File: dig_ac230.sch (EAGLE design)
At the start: 134 parts, among them IC1 74HC595D, IC101 ATMEGA32A-AU, IC102 DS1337S, IC103 MAX487CSA, IC104 74HC166D, IC2 LTV-356T, IC3 LTV-356T, IC4 LTV-356T, IC5 LTV-356T, IC6 LTV-356T, IC7 LTV-356T, IC8 LTV-356T, IC9 LTV-356T, K301 S202S02, K302 S202S02, K303 S202S02, K304 S202S02, K305 S202S02, K306 S202S02, K307 S202S02, K308 S202S02, Q1 32,768kHz, Q2 BCR191, Q3 BCR191, Q4 BCR191, Q5 BCR191, Q6 BCR191, Q7 BCR191, Q8 BCR191, Q9 BCR191, X1 RIA-73-02, X10 RIA-73-02, X11 RIA-73-02, X12 RIA-73-02, X2 RIA-73-02, X3 RIA-73-02, X4 RIA-73-02, X5 RIA-73-02, X6 RIA-73-02, X7 RIA-73-02, X8 RIA-73-02, X9 RIA-73-02

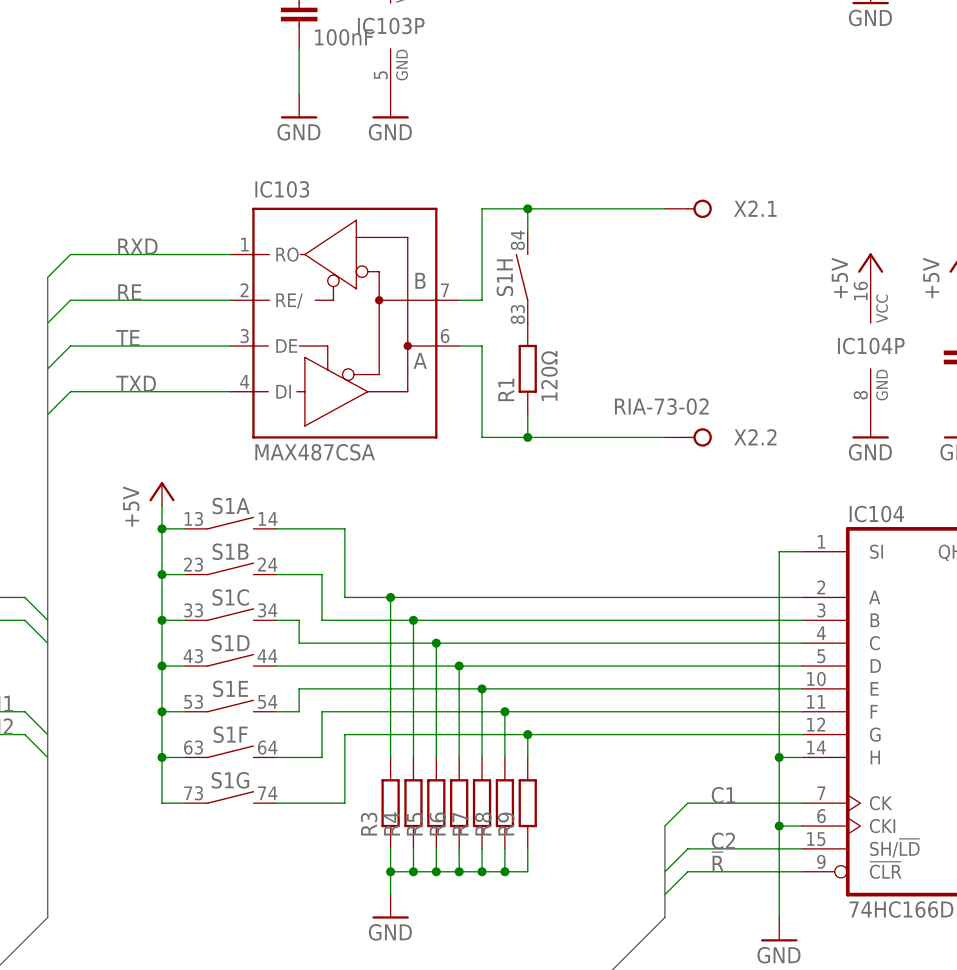
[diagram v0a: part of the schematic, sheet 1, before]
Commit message: Bauteile neu positoniert
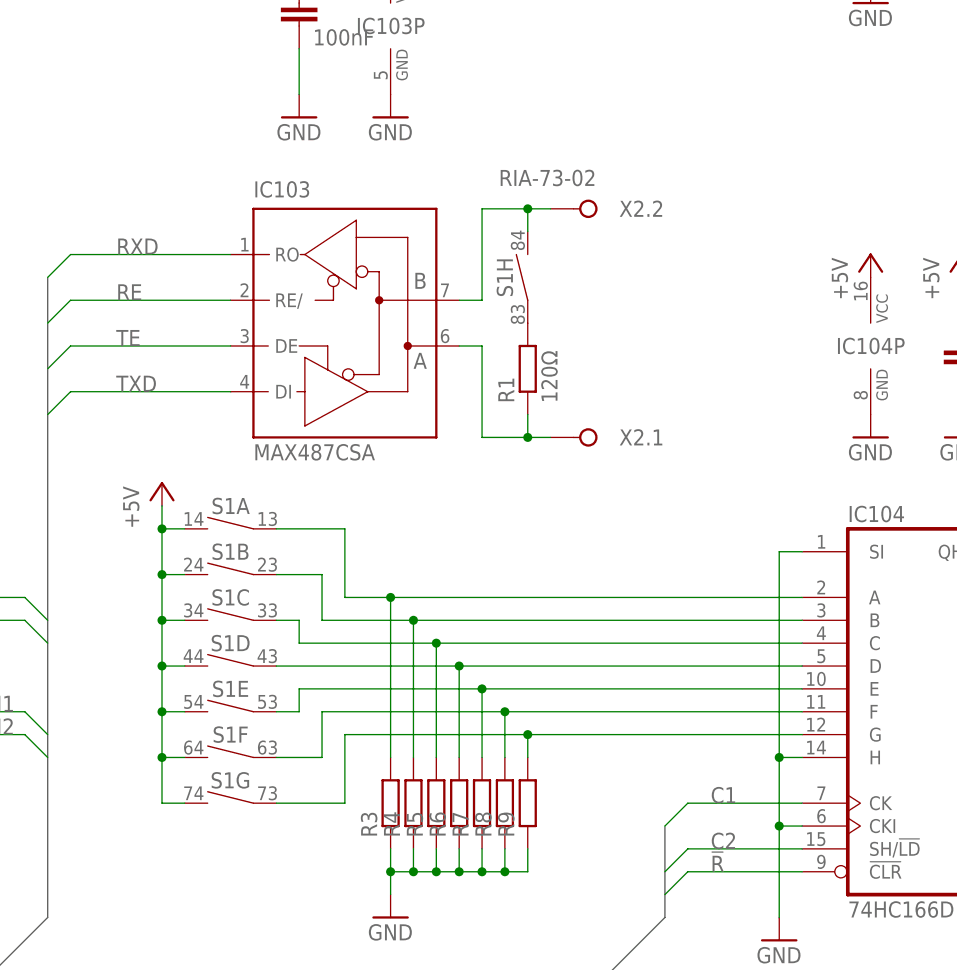
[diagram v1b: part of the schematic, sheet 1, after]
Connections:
- net GNDIO renamed N
- net N$90 renamed L
- net +5V: now also S1A.4, S1B.4, S1C.4, S1D.4, S1E.4, S1F.4, S1G.4; no longer S1A.3, S1B.3, S1C.3, S1D.3, S1E.3, S1F.3, S1G.3
- net N$20: now also X2.1.A; no longer X2.2.A
- net N$22: now also X2.2.A; no longer X2.1.A
- net N$26: now also S1A.3; no longer S1A.4
- net N$27: now also S1B.3; no longer S1B.4
- net N$28: now also S1C.3; no longer S1C.4
- net N$29: now also S1D.3; no longer S1D.4
- net N$30: now also S1E.3; no longer S1E.4
- net N$31: now also S1F.3; no longer S1F.4
- net N$32: now also S1G.3; no longer S1G.4
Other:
- moved on the sheet: X2.1, X2.2

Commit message: rev1 geroutet
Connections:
- net N$20: now also S1H.4; no longer R1.1
- net N$22: now also R1.1; no longer S1H.4
- net RE: now also IC101.(OC1A)PD5; no longer IC101.(OC1B)PD4
- net TE: now also IC101.(OC1B)PD4; no longer IC101.(OC1A)PD5
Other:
- moved on the sheet: R1, S1H
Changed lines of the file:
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@@
 <instance part="GND39" gate="1" x="292.1" y="149.86"/>
 <instance part="P+2" gate="1" x="83.82" y="167.64"/>
-<instance part="R1" gate="G$1" x="226.06" y="109.22" rot="R90"/>
+<instance part="R1" gate="G$1" x="226.06" y="119.38" rot="R270"/>
 <instance part="G1" gate="G$1" x="292.1" y="162.56"/>
 <instance part="V1" gate="G$1" x="226.06" y="175.26"/>
@@
 <instance part="S1" gate="F" x="193.04" y="66.04" rot="MR0"/>
 <instance part="S1" gate="G" x="193.04" y="60.96" rot="MR0"/>
-<instance part="S1" gate="H" x="226.06" y="119.38" rot="R90"/>
+<instance part="S1" gate="H" x="226.06" y="109.22" rot="R270"/>
 <instance part="IC104" gate="A" x="269.24" y="71.12"/>
 <instance part="R3" gate="G$1" x="210.82" y="60.96" rot="R90"/>
@@
 <wire x1="220.98" y1="111.76" x2="220.98" y2="101.6" width="0.1524" layer="91"/>
 <wire x1="220.98" y1="101.6" x2="226.06" y2="101.6" width="0.1524" layer="91"/>
-<pinref part="R1" gate="G$1" pin="1"/>
-<wire x1="226.06" y1="101.6" x2="226.06" y2="104.14" width="0.1524" layer="91"/>
 <pinref part="X2" gate=".1" pin="A"/>
-<wire x1="228.6" y1="101.6" x2="226.06" y2="101.6" width="0.1524" layer="91"/>
+<pinref part="S1" gate="H" pin="4"/>
+<wire x1="226.06" y1="101.6" x2="228.6" y2="101.6" width="0.1524" layer="91"/>
+<wire x1="226.06" y1="104.14" x2="226.06" y2="101.6" width="0.1524" layer="91"/>
 <junction x="226.06" y="101.6"/>
 </segment>
@@
 <wire x1="220.98" y1="116.84" x2="220.98" y2="127" width="0.1524" layer="91"/>
 <wire x1="220.98" y1="127" x2="226.06" y2="127" width="0.1524" layer="91"/>
-<pinref part="S1" gate="H" pin="4"/>
-<wire x1="226.06" y1="124.46" x2="226.06" y2="127" width="0.1524" layer="91"/>
 <pinref part="X2" gate=".2" pin="A"/>
-<wire x1="228.6" y1="127" x2="226.06" y2="127" width="0.1524" layer="91"/>
+<pinref part="R1" gate="G$1" pin="1"/>
+<wire x1="226.06" y1="127" x2="228.6" y2="127" width="0.1524" layer="91"/>
+<wire x1="226.06" y1="127" x2="226.06" y2="124.46" width="0.1524" layer="91"/>
 <junction x="226.06" y="127"/>
 </segment>
@@
 </segment>
 <segment>
+<pinref part="IC101" gate="G$1" pin="(OC1B)PD4"/>
+<wire x1="93.98" y1="66.04" x2="106.68" y2="66.04" width="0.1524" layer="91"/>
+<wire x1="106.68" y1="66.04" x2="109.22" y2="63.5" width="0.1524" layer="91"/>
+<label x="96.52" y="66.04" size="1.778" layer="95"/>
+</segment>
+</net>
+<net name="RE" class="0">
+<segment>
+<pinref part="IC103" gate="A" pin="RE/"/>
+<wire x1="193.04" y1="116.84" x2="175.26" y2="116.84" width="0.1524" layer="91"/>
+<wire x1="175.26" y1="116.84" x2="172.72" y2="114.3" width="0.1524" layer="91"/>
+<label x="180.34" y="116.84" size="1.778" layer="95"/>
+</segment>
+<segment>
 <pinref part="IC101" gate="G$1" pin="(OC1A)PD5"/>
 <wire x1="93.98" y1="68.58" x2="106.68" y2="68.58" width="0.1524" layer="91"/>
@@
 </segment>
 </net>
-<net name="RE" class="0">
-<segment>
-<pinref part="IC103" gate="A" pin="RE/"/>
-<wire x1="193.04" y1="116.84" x2="175.26" y2="116.84" width="0.1524" layer="91"/>
-<wire x1="175.26" y1="116.84" x2="172.72" y2="114.3" width="0.1524" layer="91"/>
-<label x="180.34" y="116.84" size="1.778" layer="95"/>
-</segment>
-<segment>
-<pinref part="IC101" gate="G$1" pin="(OC1B)PD4"/>
-<wire x1="93.98" y1="66.04" x2="106.68" y2="66.04" width="0.1524" layer="91"/>
-<wire x1="106.68" y1="66.04" x2="109.22" y2="63.5" width="0.1524" layer="91"/>
-<label x="96.52" y="66.04" size="1.778" layer="95"/>
-</segment>
-</net>

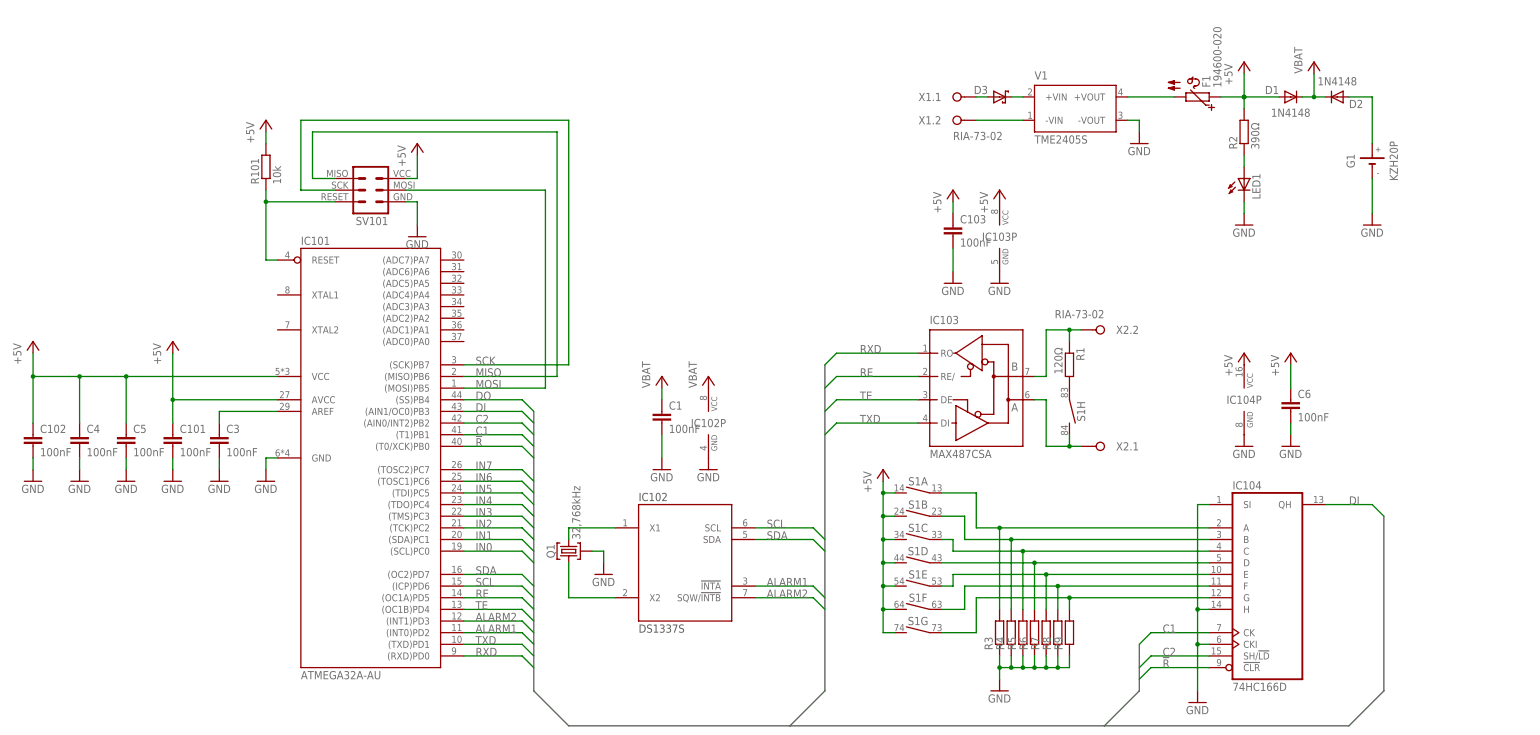
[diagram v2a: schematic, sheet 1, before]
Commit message: Statusleds, Temperatur- und Batteriemessung hinzugefügt
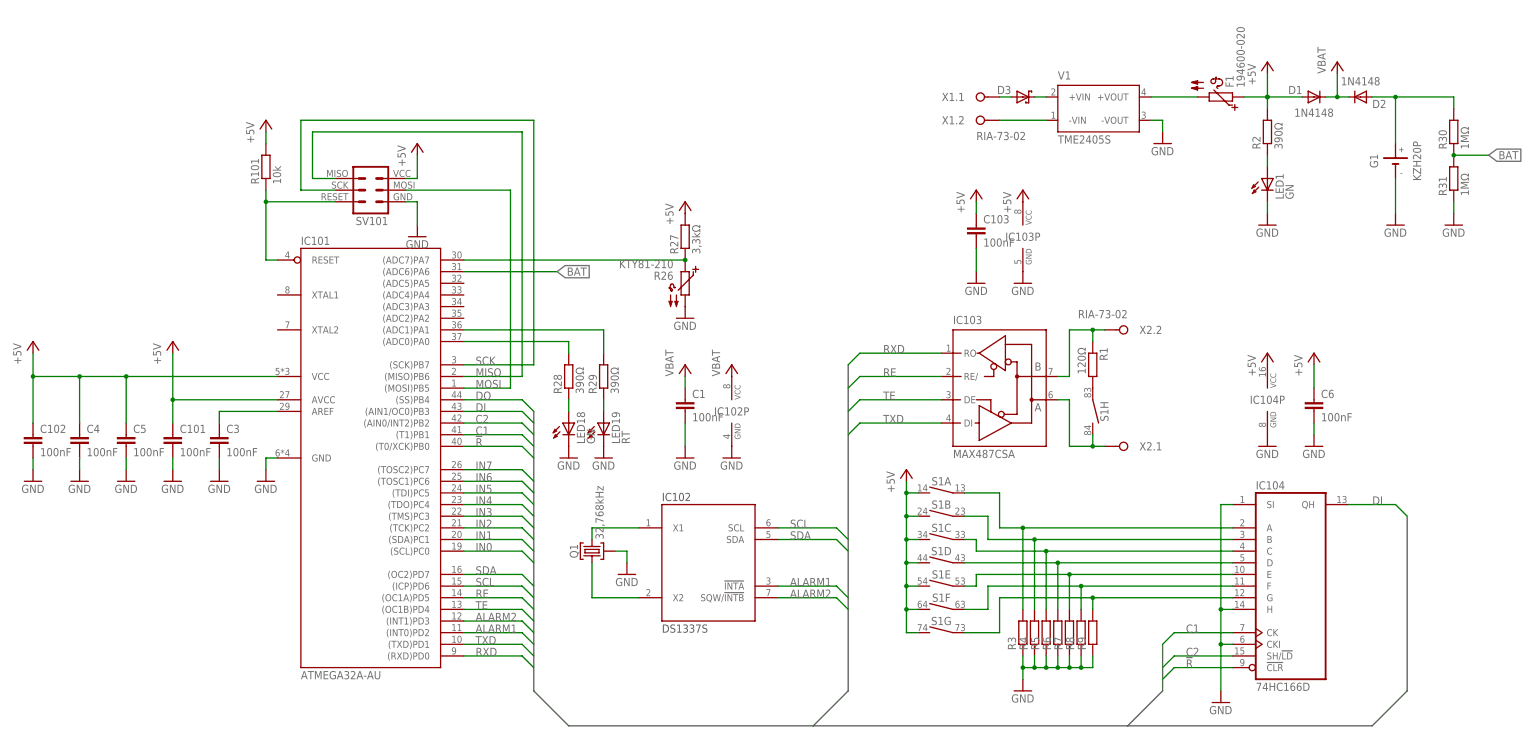
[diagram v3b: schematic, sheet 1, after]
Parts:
- added LED18: GN, led:LED3MM
- added LED19: RT, led:LED3MM
- added R26: KTY81-210, sensor:KTY81-210
- added R27: 3,3kΩ, passiv:R_0805
- added R28, R29: 390Ω, passiv:R_0805
- added R30, R31: 1MΩ, passiv:R_0805
- LED1, LED10, LED11, LED12, LED13, LED14, LED15, LED16, LED17, LED2, LED3, LED4, LED5, LED6, LED7, LED8, LED9: value (none) -> GN
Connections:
- new net BAT: IC101.(ADC6)PA6, R30.1, R31.2
- new net N$61: IC101.(ADC7)PA7, R26.1, R27.1
- new net N$62: LED18.A, R28.1
- new net N$63: LED19.A, R29.1
- new net N$90: IC101.(ADC0)PA0, R28.2
- new net N$92: IC101.(ADC1)PA1, R29.2
- net +5V: now also R27.2
- net GND: now also LED18.C, LED19.C, R26.2, R31.1
- net N$21: now also R30.2
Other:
- moved on the sheet: C1, C103, C6, D1, D2, D3, F1, G1, IC102, IC102P, IC103, IC103P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

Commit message: Schematik übersichtlicher gemacht; Bauteile neu benannt; Werte ergänzt
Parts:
- removed C1, C2, C3, C4, C5, C6: 100nF, passiv:C_0805
- removed D1, D10, D11, D2, D4, D5, D6, D7, D8, D9: 1N4148, diode:DIODE-MINIMELF
- removed D201, D202, D203, D204, D205, D206, D207, D208: DL4007, diode:DIODE-MELF
- removed D3: (no value), diode:SHOTKY-DIODE-MELF
- removed F1: 194600-020, sicherung:194600-020
- removed G1: KZH20P, batterie:KZH20P
- removed IC1: 74HC595D, ic-logik:74HC595D
- removed IC101: ATMEGA32A-AU, ic-mcu:ATMEGA32A-AU
- removed IC102: DS1337S, ic-controller:DS1337S
- removed IC103: MAX487CSA, ic-wandler:MAX487CSA
- removed IC104: 74HC166D, ic-logik:74HC166D
- removed IC2, IC3, IC4, IC5, IC6, IC7, IC8, IC9: LTV-356T, ic-optokoppler:LTV-356T
- removed K301, K302, K303, K304, K305, K306, K307, K308: S202S02, relais:S202S02
- removed LED1, LED10, LED11, LED12, LED13, LED14, LED15, LED16, LED17, LED18, LED2, LED3, LED4, LED5, LED6, LED7, LED8, LED9: GN, led:LED3MM
- removed LED19: RT, led:LED3MM
- removed Q1: 32,768kHz, passiv:QM_
- removed Q2, Q3, Q4, Q5, Q6, Q7, Q8, Q9: BCR191, transistor:PNP2R-SOT23-BEC
- removed R1: 120Ω, passiv:R_0805
- removed R10, R11, R12, R13, R14, R15, R16, R17, R2, R28, R29: 390Ω, passiv:R_0805
- removed R18, R19, R20, R21, R22, R23, R24, R25: 120kΩ, passiv:R_1206
- removed R26: KTY81-210, sensor:KTY81-210
- removed R27: 3,3kΩ, passiv:R_0805
- removed R3, R4, R5, R6, R7, R8, R9: (no value), passiv:R_0805
- removed R30, R31: 1MΩ, passiv:R_0805
- removed S1: (no value), schalter:DP08
- removed SV101: (no value), stecker:AVR_ISP6L
- removed V1: TME2405S, schaltregler:TME2405S
- removed X1, X10, X11, X12, X2, X3, X4, X5, X6, X7, X8, X9: RIA-73-02, anschluss:RIA-73-02
- added C104, C201, C202, C203, C204, C205: 100nF, passiv:C_0805
- added D101: TMBAT49, diode:SHOTKY-DIODE-MELF
- added D102, D103, D302, D304, D306, D308, D310, D312, D314, D316: 1N4148, diode:DIODE-MINIMELF
- added D301, D303, D305, D307, D309, D311, D313, D315: DL4007, diode:DIODE-MELF
- added F101: 194600-020, sicherung:194600-020
- added G101: KZH20P, batterie:KZH20P
- added IC201: ATMEGA32A-AU, ic-mcu:ATMEGA32A-AU
- added IC202: DS1337S, ic-controller:DS1337S
- added IC203: MAX487CSA, ic-wandler:MAX487CSA
- added IC204: 74HC166D, ic-logik:74HC166D
- added IC301, IC302, IC303, IC304, IC305, IC306, IC307, IC308: LTV-356T, ic-optokoppler:LTV-356T
- added IC401: 74HC595D, ic-logik:74HC595D
- added K401, K402, K403, K404, K405, K406, K407, K408: S202S02, relais:S202S02
- added L101, L201, L301, L302, L303, L304, L305, L306, L307, L308, L401, L402, L403, L404, L405, L406, L407, L408: GN, led:LED3MM
- added L202: RT, led:LED3MM
- added Q201: 32,768kHz, passiv:QM_
- added Q301, Q302, Q303, Q304, Q305, Q306, Q307, Q308: BCR191, transistor:PNP2R-SOT23-BEC
- added R102, R103: 1MΩ, passiv:R_0805
- added R209, R210, R211, R212, R213: 22kΩ, passiv:R_0805
- added R309, R312, R315, R318, R321, R324: 390Ω, passiv:R_0805
- added R310, R311, R313, R314, R316, R317, R319, R320, R322, R323: 120kΩ, passiv:R_1206
- added R401, R402, R403, R404, R405, R406, R407, R408: 180Ω, passiv:R_0805
- added S201: (no value), schalter:DP08
- added V101: TME2405S, schaltregler:TME2405S
- added X101, X202, X301, X302, X303, X304, X305, X401, X402, X403, X404, X405: RIA-73-02, anschluss:RIA-73-02
- added X201: ISP, stecker:AVR_ISP6L
- R101: value 10k -> 390Ω
- R201: value 120kΩ -> 10k; device passiv:R_1206 -> passiv:R_0805
- R202, R203: value 120kΩ -> 390Ω; device passiv:R_1206 -> passiv:R_0805
- R204: value 120kΩ -> 3,3kΩ; device passiv:R_1206 -> passiv:R_0805
- R205: value 120kΩ -> KTY81-210; device passiv:R_1206 -> sensor:KTY81-210
- R206: value 120kΩ -> 120Ω; device passiv:R_1206 -> passiv:R_0805
- R207, R208: value 120kΩ -> 22kΩ; device passiv:R_1206 -> passiv:R_0805
- R301, R302, R304, R305, R307, R308: value 180Ω -> 120kΩ; device passiv:R_0805 -> passiv:R_1206
- R303, R306: value 180Ω -> 390Ω
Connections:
- removed net VCC: C1.1, D1.K, D2.K, IC102P.VCC
- new net N$64: C104.1, D102.K, D103.K, IC202P.VCC
- net !R: now also IC201.(T0/XCK)PB0, IC204A.!CLR, IC401A.!SCLR; no longer IC101.(T0/XCK)PB0, IC104A.!CLR, IC1A.!SCLR
- net +5V: now also C201.1, C202.1, C203.1, C204.1, D102.A, F101.1, IC201.AVCC, IC201.VCC, IC203P.VCC, IC204P.VCC, IC401P.VCC, Q301.E, Q302.E, Q303.E, Q304.E, Q305.E, Q306.E, Q307.E, Q308.E, R201.2, R204.2, S201A.4, S201B.4, S201C.4, S201D.4, S201E.4, S201F.4, S201G.4, X201.VCC; no longer C2.1, C4.1, C5.1, C6.1, D1.A, F1.1, IC101.AVCC, IC101.VCC, IC103P.VCC, IC104P.VCC, IC1P.VCC, Q2.E, Q3.E, Q4.E, Q5.E, Q6.E, Q7.E, Q8.E, Q9.E, R2.2, R27.2, S1A.4, S1B.4, S1C.4, S1D.4, S1E.4, S1F.4, S1G.4, SV101.VCC
- net ALARM1: now also IC201.(INT0)PD2, IC202A.!INTA; no longer IC101.(INT0)PD2, IC102A.!INTA
- net ALARM2: now also IC201.(INT1)PD3, IC202A.SQW/!INTB; no longer IC101.(INT1)PD3, IC102A.SQW/!INTB
- net BAT: now also IC201.(ADC6)PA6, R102.1, R103.2; no longer IC101.(ADC6)PA6, R30.1, R31.2
- net C1: now also IC201.(T1)PB1, IC204A.CK, IC401A.SCK; no longer IC101.(T1)PB1, IC104A.CK, IC1A.SCK
- net C2: now also IC201.(AIN0/INT2)PB2, IC204A.SH/!LD, IC401A.RCK; no longer IC101.(AIN0/INT2)PB2, IC104A.SH/!LD, IC1A.RCK
- net DI: now also IC201.(AIN1/OC0)PB3, IC204A.QH; no longer IC101.(AIN1/OC0)PB3, IC104A.QH
- net DO: now also IC201.(SS)PB4, IC401A.SI; no longer IC101.(SS)PB4, IC1A.SI
- net GND: now also C104.2, C201.2, C202.2, C203.2, C204.2, C205.2, G101.-, IC201.GND, IC202P.GND, IC203P.GND, IC204A.CKI, IC204A.H, IC204A.SI, IC204P.GND, IC301.E, IC302.E, IC303.E, IC304.E, IC305.E, IC306.E, IC307.E, IC308.E, IC401A.!OE, IC401P.GND, K401.K, K402.K, K403.K, K404.K, K405.K, K406.K, K407.K, K408.K, L101.C, L201.C, L202.C, L301.C, L302.C, L303.C, L304.C, L305.C, L306.C, L307.C, L308.C, Q201.G, R103.1, R205.2, R207.1, R208.1, R209.1, R210.1, R211.1, R212.1, R213.1, V101.-VOUT, X201.GND; no longer C1.2, C2.2, C3.2, C4.2, C5.2, C6.2, G1.-, IC101.GND, IC102P.GND, IC103P.GND, IC104A.CKI, IC104A.H, IC104A.SI, IC104P.GND, IC1A.!OE, IC1P.GND, IC2.E, IC3.E, IC4.E, IC5.E, IC6.E, IC7.E, IC8.E, IC9.E, K301.K, K302.K, K303.K, K304.K, K305.K, K306.K, K307.K, K308.K, LED1.C, LED10.C, LED11.C, LED12.C, LED13.C, LED14.C, LED15.C, LED16.C, LED17.C, LED18.C, LED19.C, Q1.G, R26.2, R3.1, R31.1, R4.1, R5.1, R6.1, R7.1, R8.1, R9.1, SV101.GND, V1.-VOUT
- net IN0: now also IC201.(SCL)PC0, Q301.C, R303.2; no longer IC101.(SCL)PC0, Q5.C, R13.2
- net IN1: now also IC201.(SDA)PC1, Q302.C, R306.2; no longer IC101.(SDA)PC1, Q4.C, R12.2
- net IN2: now also IC201.(TCK)PC2, Q303.C, R309.2; no longer IC101.(TCK)PC2, Q3.C, R11.2
- net IN3: now also IC201.(TMS)PC3, Q304.C, R312.2; no longer IC101.(TMS)PC3, Q2.C, R10.2
- net IN4: now also IC201.(TDO)PC4, Q305.C, R315.2; no longer IC101.(TDO)PC4, Q6.C, R14.2
- net IN5: now also IC201.(TDI)PC5, Q306.C, R318.2; no longer IC101.(TDI)PC5, Q7.C, R15.2
- net IN6: now also IC201.(TOSC1)PC6, Q307.C, R321.2; no longer IC101.(TOSC1)PC6, Q8.C, R16.2
- net IN7: now also IC201.(TOSC2)PC7, Q308.C, R324.2; no longer IC101.(TOSC2)PC7, Q9.C, R17.2
- net L: now also K401.DS2, K402.DS2, K403.DS2, K404.DS2, K405.DS2, K406.DS2, K407.DS2, K408.DS2, X401.1.A, X401.2.A; no longer K301.DS2, K302.DS2, K303.DS2, K304.DS2, K305.DS2, K306.DS2, K307.DS2, K308.DS2, X12.1.A, X12.2.A
- net MISO: now also IC201.(MISO)PB6, X201.MISO; no longer IC101.(MISO)PB6, SV101.MISO
- net MOSI: now also IC201.(MOSI)PB5, X201.MOSI; no longer IC101.(MOSI)PB5, SV101.MOSI
- net N: now also R302.1, R305.1, R308.1, R311.1, R314.1, R317.1, R320.1, R323.1, X301.1.A, X301.2.A; no longer R18.1, R19.1, R20.1, R21.1, R22.1, R23.1, R24.1, R25.1, X7.1.A, X7.2.A
- net N$1: now also D301.K, D302.K, IC301.A; no longer D201.K, D4.K, IC2.A
- net N$10: now also D310.A, IC305.K, R313.2; no longer D8.A, IC6.K, R205.2
- net N$100: now also D313.A, X305.2.A; no longer D207.A, X6.2.A
- net N$101: now also D315.A, X305.1.A; no longer D208.A, X6.1.A
- net N$103: now also L401.A, R401.2; no longer LED2.A, R301.2
- net N$104: now also L402.A, R402.2; no longer LED3.A, R302.2
- net N$105: now also L403.A, R403.2; no longer LED4.A, R303.2
- net N$106: now also L404.A, R404.2; no longer LED5.A, R304.2
- net N$107: now also L405.A, R405.2; no longer LED6.A, R305.2
- net N$108: now also L406.A, R406.2; no longer LED7.A, R306.2
- net N$109: now also L407.A, R407.2; no longer LED8.A, R307.2
- net N$11: now also D311.K, D312.K, IC306.A; no longer D206.K, D9.K, IC7.A
- net N$110: now also L408.A, R408.2; no longer LED9.A, R308.2
- net N$12: now also D312.A, IC306.K, R316.2; no longer D9.A, IC7.K, R206.2
- net N$126: now also IC202A.X1, Q201.2; no longer IC102A.X1, Q1.2
- net N$127: now also IC202A.X2, Q201.1; no longer IC102A.X2, Q1.1
- net N$13: now also D313.K, D314.K, IC307.A; no longer D10.K, D207.K, IC8.A
- net N$14: now also D314.A, IC307.K, R319.2; no longer D10.A, IC8.K, R207.2
- net N$15: now also D315.K, D316.K, IC308.A; no longer D11.K, D208.K, IC9.A
- net N$16: now also D316.A, IC308.K, R322.2; no longer D11.A, IC9.K, R208.2
- net N$17: now also K401.A, L401.C; no longer K301.A, LED2.C
- net N$18: now also K402.A, L402.C; no longer K302.A, LED3.C
- net N$19: now also V101.-VIN, X101.2.A; no longer V1.-VIN, X1.2.A
- net N$2: now also D302.A, IC301.K, R301.2; no longer D4.A, IC2.K, R201.2
- net N$20: now also IC203A.A, S201H.4, X202.1.A; no longer IC103A.A, S1H.4, X2.1.A
- net N$21: now also D103.A, G101.+, R102.2; no longer D2.A, G1.+, R30.2
- net N$22: now also IC203A.B, R206.1, X202.2.A; no longer IC103A.B, R1.1, X2.2.A
- net N$23: now also D101.K, V101.+VIN; no longer D3.K, V1.+VIN
- net N$24: now also D101.A, X101.1.A; no longer D3.A, X1.1.A
- net N$25: now also C205.1, IC201.AREF; no longer C3.1, IC101.AREF
- net N$26: now also IC204A.A, R207.2, S201A.3; no longer IC104A.A, R3.2, S1A.3
- net N$27: now also IC204A.B, R208.2, S201B.3; no longer IC104A.B, R4.2, S1B.3
- net N$28: now also IC204A.C, R209.2, S201C.3; no longer IC104A.C, R5.2, S1C.3
- net N$29: now also IC204A.D, R210.2, S201D.3; no longer IC104A.D, R6.2, S1D.3
- net N$3: now also D303.K, D304.K, IC302.A; no longer D202.K, D5.K, IC3.A
- net N$30: now also IC204A.E, R211.2, S201E.3; no longer IC104A.E, R7.2, S1E.3
- net N$31: now also IC204A.F, R212.2, S201F.3; no longer IC104A.F, R8.2, S1F.3
- net N$32: now also IC204A.G, R213.2, S201G.3; no longer IC104A.G, R9.2, S1G.3
- net N$33: now also R206.2, S201H.3; no longer R1.2, S1H.3
- net N$34: now also L304.A, R312.1; no longer LED10.A, R10.1
- net N$35: now also R301.1, R302.2; no longer R18.2, R201.1
- net N$36: now also L303.A, R309.1; no longer LED11.A, R11.1
- net N$37: now also R304.1, R305.2; no longer R19.2, R202.1
- net N$38: now also L302.A, R306.1; no longer LED12.A, R12.1
- net N$39: now also R307.1, R308.2; no longer R20.2, R203.1
- net N$4: now also D304.A, IC302.K, R304.2; no longer D5.A, IC3.K, R202.2
- net N$40: now also L301.A, R303.1; no longer LED13.A, R13.1
- net N$41: now also F101.2, V101.+VOUT; no longer F1.2, V1.+VOUT
- net N$42: now also IC201.RESET, R201.1, X201.RESET; no longer IC101.RESET, R101.1, SV101.RESET
- net N$43: now also K403.A, L403.C; no longer K303.A, LED4.C
- net N$44: now also L101.A, R101.1; no longer LED1.A, R2.1
- net N$45: now also K404.A, L404.C; no longer K304.A, LED5.C
- net N$46: now also K405.A, L405.C; no longer K305.A, LED6.C
- net N$47: now also K406.A, L406.C; no longer K306.A, LED7.C
- net N$48: now also K407.A, L407.C; no longer K307.A, LED8.C
- net N$49: now also K408.A, L408.C; no longer K308.A, LED9.C
- net N$5: now also D305.K, D306.K, IC303.A; no longer D203.K, D6.K, IC4.A
- net N$50: now also R310.1, R311.2; no longer R204.1, R21.2
- net N$51: now also IC401A.QA, R401.1; no longer IC1A.QA, R301.1
- net N$52: now also IC304.C, Q304.B; no longer IC5.C, Q2.B
- net N$53: now also IC401A.QB, R402.1; no longer IC1A.QB, R302.1
- net N$54: now also IC401A.QC, R403.1; no longer IC1A.QC, R303.1
- net N$55: now also L305.A, R315.1; no longer LED14.A, R14.1
- net N$56: now also IC401A.QD, R404.1; no longer IC1A.QD, R304.1
- net N$57: now also R313.1, R314.2; no longer R205.1, R22.2
- net N$58: now also IC401A.QE, R405.1; no longer IC1A.QE, R305.1
- net N$59: now also IC401A.QF, R406.1; no longer IC1A.QF, R306.1
- net N$6: now also D306.A, IC303.K, R307.2; no longer D6.A, IC4.K, R203.2
- net N$60: now also IC401A.QG, R407.1; no longer IC1A.QG, R307.1
- net N$61: now also IC201.(ADC7)PA7, R204.1, R205.1; no longer IC101.(ADC7)PA7, R26.1, R27.1
- net N$62: now also L201.A, R202.1; no longer LED18.A, R28.1
- net N$63: now also L202.A, R203.1; no longer LED19.A, R29.1
- net N$65: now also L306.A, R318.1; no longer LED15.A, R15.1
- net N$66: now also IC401A.QH, R408.1; no longer IC1A.QH, R308.1
- net N$67: now also R316.1, R317.2; no longer R206.1, R23.2
- net N$68: now also K401.DS1, X402.1.A; no longer K301.DS1, X8.1.A
- net N$69: now also L307.A, R321.1; no longer LED16.A, R16.1
- net N$7: now also D307.K, D308.K, IC304.A; no longer D204.K, D7.K, IC5.A
- net N$70: now also IC303.C, Q303.B; no longer IC4.C, Q3.B
- net N$71: now also R319.1, R320.2; no longer R207.1, R24.2
- net N$72: now also K402.DS1, X402.2.A; no longer K302.DS1, X8.2.A
- net N$73: now also IC302.C, Q302.B; no longer IC3.C, Q4.B
- net N$74: now also K403.DS1, X403.1.A; no longer K303.DS1, X9.1.A
- net N$75: now also IC301.C, Q301.B; no longer IC2.C, Q5.B
- net N$76: now also K404.DS1, X403.2.A; no longer K304.DS1, X9.2.A
- net N$77: now also L308.A, R324.1; no longer LED17.A, R17.1
- net N$78: now also K405.DS1, X404.1.A; no longer K305.DS1, X10.1.A
- net N$79: now also R322.1, R323.2; no longer R208.1, R25.2
- net N$8: now also D308.A, IC304.K, R310.2; no longer D7.A, IC5.K, R204.2
- net N$80: now also IC305.C, Q305.B; no longer IC6.C, Q6.B
- net N$81: now also IC306.C, Q306.B; no longer IC7.C, Q7.B
- net N$82: now also K406.DS1, X404.2.A; no longer K306.DS1, X10.2.A
- net N$83: now also IC307.C, Q307.B; no longer IC8.C, Q8.B
- net N$84: now also K407.DS1, X405.1.A; no longer K307.DS1, X11.1.A
- net N$85: now also IC308.C, Q308.B; no longer IC9.C, Q9.B
- net N$86: now also D301.A, X302.2.A; no longer D201.A, X3.2.A
- net N$87: now also D303.A, X302.1.A; no longer D202.A, X3.1.A
- net N$88: now also D305.A, X303.2.A; no longer D203.A, X4.2.A
- net N$89: now also K408.DS1, X405.2.A; no longer K308.DS1, X11.2.A
- net N$9: now also D309.K, D310.K, IC305.A; no longer D205.K, D8.K, IC6.A
- net N$90: now also IC201.(ADC0)PA0, R202.2; no longer IC101.(ADC0)PA0, R28.2
- net N$91: now also D307.A, X303.1.A; no longer D204.A, X4.1.A
- net N$92: now also IC201.(ADC1)PA1, R203.2; no longer IC101.(ADC1)PA1, R29.2
- net N$94: now also D309.A, X304.2.A; no longer D205.A, X5.2.A
- net N$97: now also D311.A, X304.1.A; no longer D206.A, X5.1.A
- net RE: now also IC201.(OC1A)PD5, IC203A.RE/; no longer IC101.(OC1A)PD5, IC103A.RE/
- net RXD: now also IC201.(RXD)PD0, IC203A.RO; no longer IC101.(RXD)PD0, IC103A.RO
- net SCK: now also IC201.(SCK)PB7, X201.SCK; no longer IC101.(SCK)PB7, SV101.SCK
- net SCL: now also IC201.(ICP)PD6, IC202A.SCL; no longer IC101.(ICP)PD6, IC102A.SCL
- net SDA: now also IC201.(OC2)PD7, IC202A.SDA; no longer IC101.(OC2)PD7, IC102A.SDA
- net TE: now also IC201.(OC1B)PD4, IC203A.DE; no longer IC101.(OC1B)PD4, IC103A.DE
- net TXD: now also IC201.(TXD)PD1, IC203A.DI; no longer IC101.(TXD)PD1, IC103A.DI

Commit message: Bauteile wegen Beschriftung ausgetauscht
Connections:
- net N renamed GNDIO
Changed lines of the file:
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@@
 </segment>
 </net>
-<net name="N" class="0">
+<net name="GNDIO" class="0">
 <segment>
 <pinref part="R308" gate="G$1" pin="1"/>
